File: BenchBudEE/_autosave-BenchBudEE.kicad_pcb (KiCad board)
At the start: 4 copper layers, 165.1 x 63.5 mm, 68 parts, among them K1 1461069-5, P1 24 pin Mini-fit Jr, P2 CONN_3X2, P3 CONN_2, P4 12 pin terminal block, P5 3 Pin TB, Q1 2N3904, Q2 DMN65D8L-7, Q3 B130-13-F, Q4 B130-13-F, U1 LTV-816S, U10 MCP4801, U2 MCP3901, U3 LMT84, U4 OPA4170

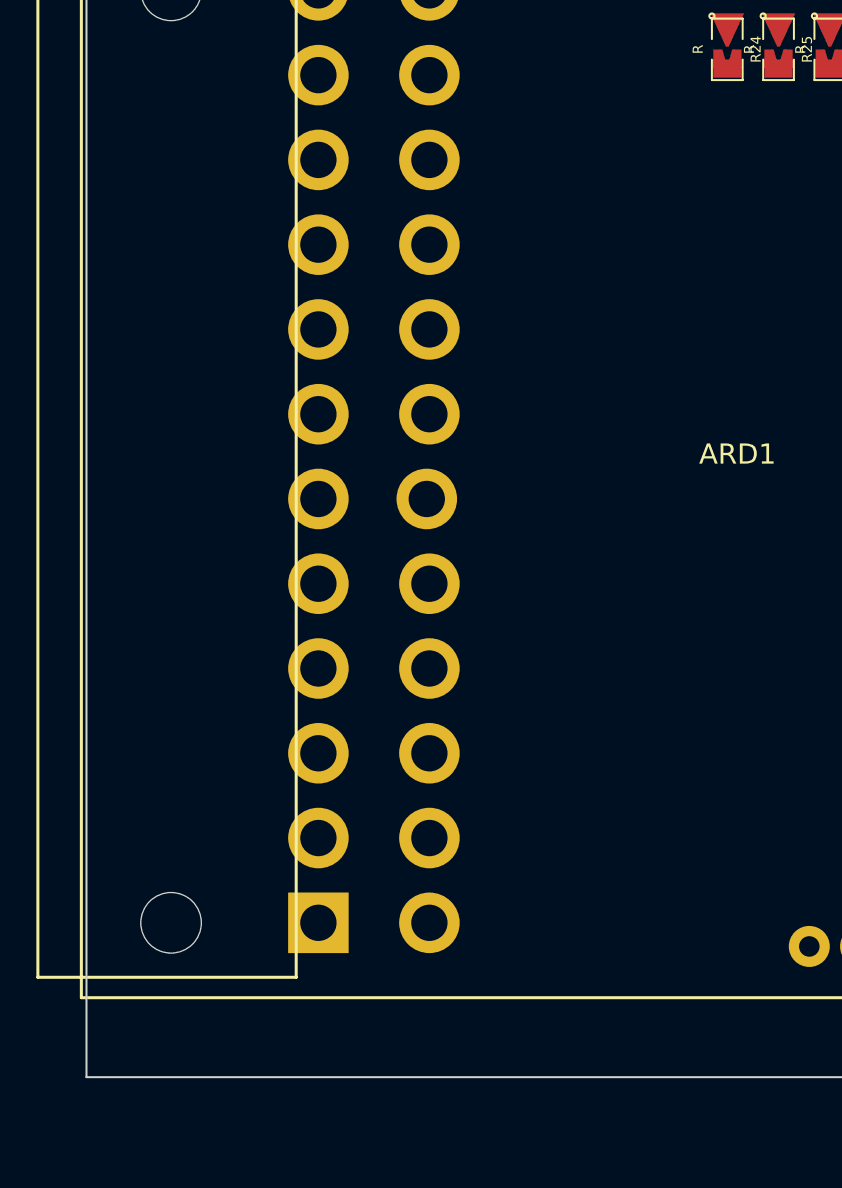
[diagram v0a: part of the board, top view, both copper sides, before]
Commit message: Associating and Placing the Power protection module
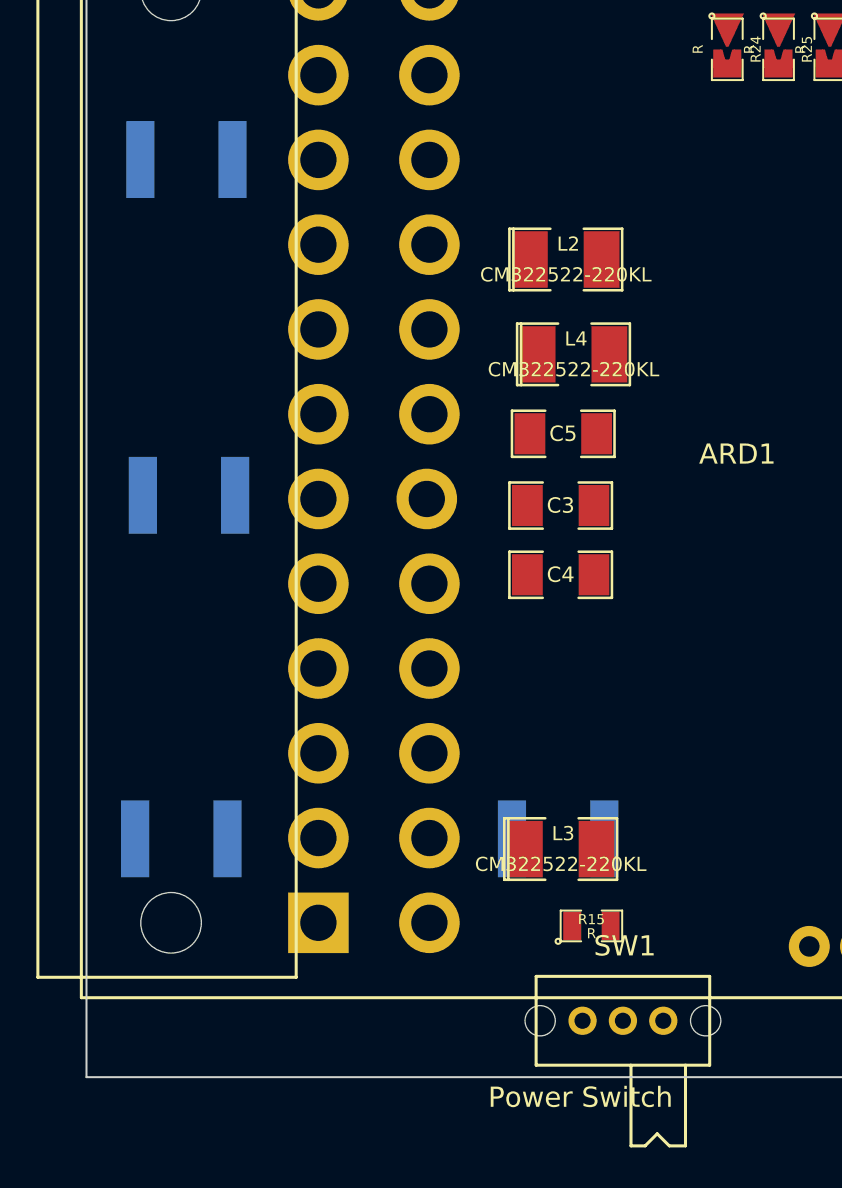
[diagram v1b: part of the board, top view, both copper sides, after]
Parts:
- added C3: C, SM1206, F.Cu at (148.7, 133.2)
- added C4: C, SM1206, F.Cu at (148.7, 136.7)
- added C5: C, SM1206, F.Cu at (148.8, 129.7)
- added L2: CM322522-220KL, SM1210L, F.Cu at (149.0, 121.0)
- added L3: CM322522-220KL, SM1210L, F.Cu at (148.7, 150.2)
- added L4: CM322522-220KL, SM1210L, F.Cu at (149.4, 125.7)
- added R15: R, SM0805, F.Cu at (150.2, 154.1)
- added SW1: Power Switch, BB_Switch, F.Cu at (147.7, 158.8)
- added TH1: MINISMDC050F-2, SM1812, B.Cu at (129.9, 149.7)
- added TH2: MINISMDC050F-2, SM1812, B.Cu at (130.3, 132.7)
- added TH3: MINISMDC050F-2, SM1812, B.Cu at (130.2, 116.1)
- added TH4: MINISMDC050F-2, SM1812, B.Cu at (148.6, 149.7)
